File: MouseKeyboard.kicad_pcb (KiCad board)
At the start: 2 copper layers, 79.4 x 62.2 mm, 20 parts, among them IC1 ATMEGA328P-P, J1 USB, SW1 SW_PUSH, SW2 SW_PUSH, SW3 SW_PUSH, SW4 SW_PUSH, SW5 SW_PUSH, SW6 SW_PUSH, SW7 SW_PUSH, SW8 SPST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

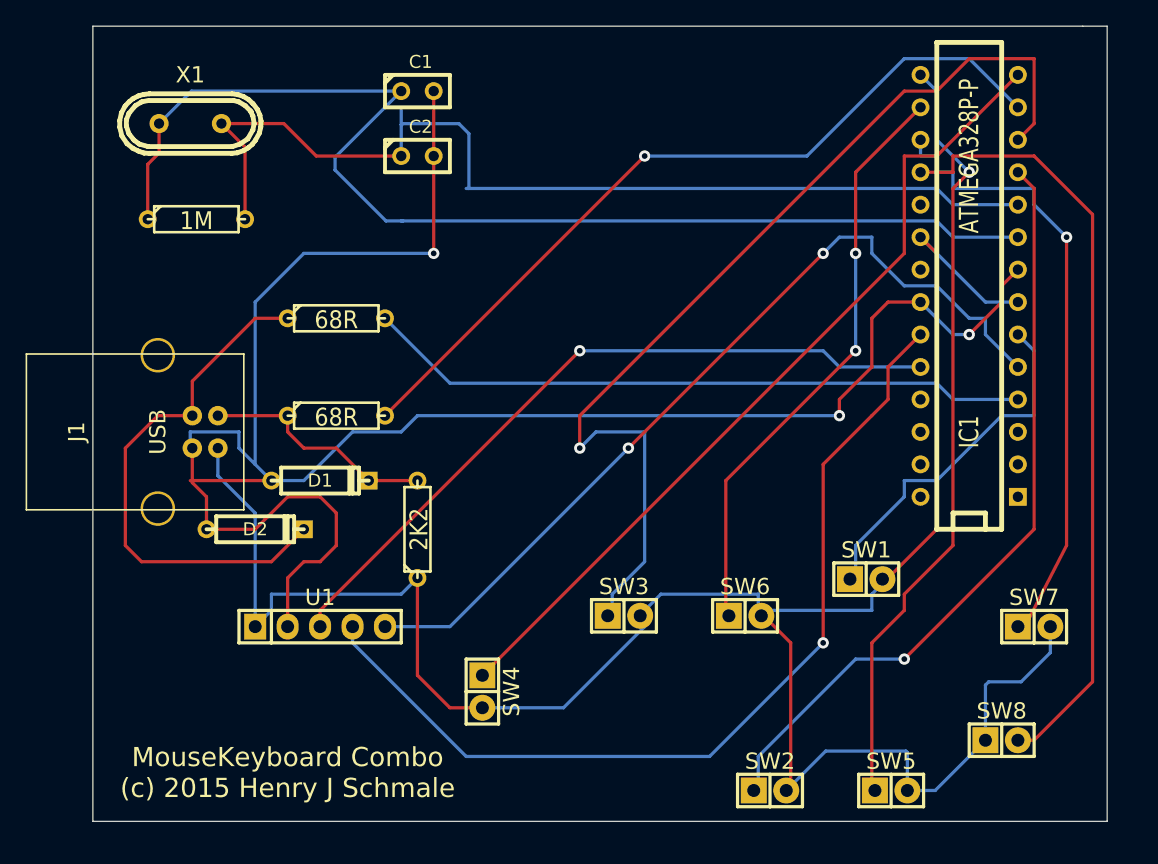
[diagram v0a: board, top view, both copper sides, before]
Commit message: Improved PCB Design
* Reduced Size of board by ~20%
* Rerouted, and it passes the design check
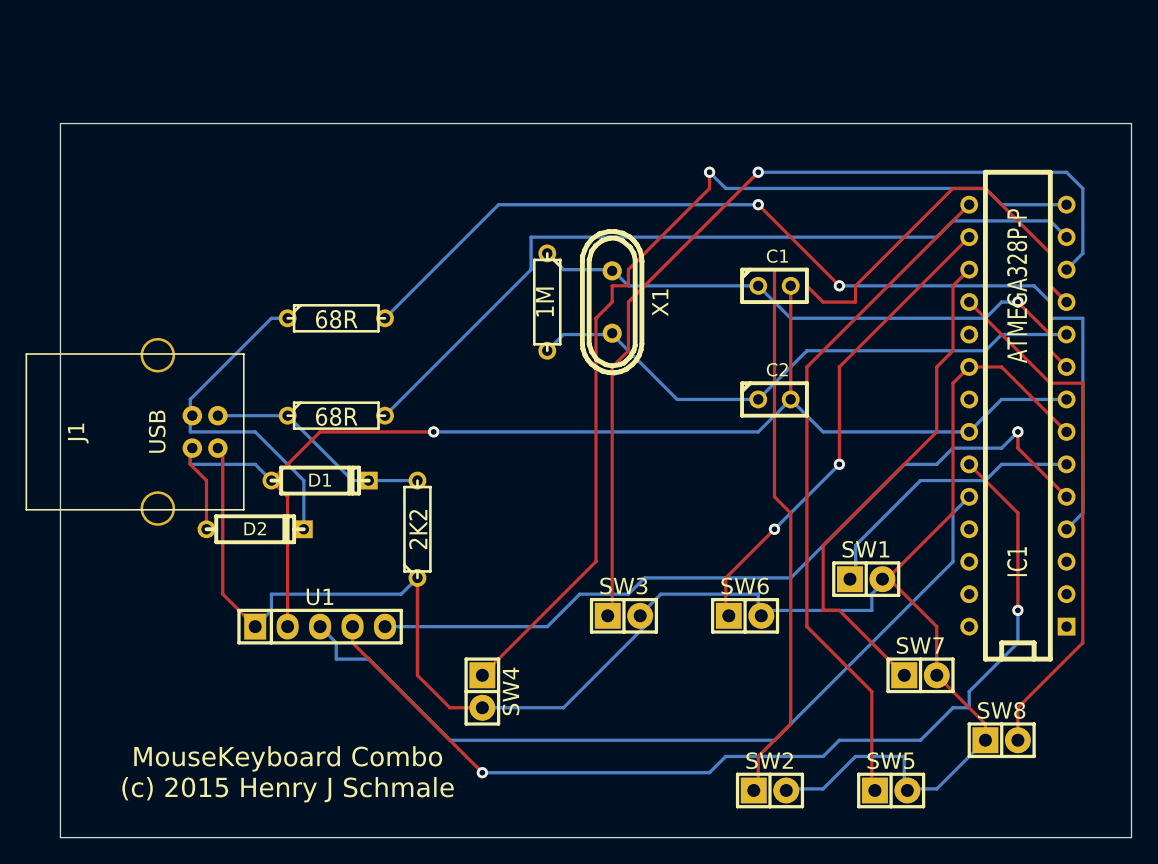
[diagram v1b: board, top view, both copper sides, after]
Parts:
- moved X1 35.9 mm to (142.2, 92.7), turned to 270 degrees
- moved C2 33.8 mm to (154.9, 100.3)
- moved C1 31.8 mm to (154.9, 91.4)
- moved R4 28.2 mm to (137.2, 92.7), turned to 270 degrees
- moved IC1 10.9 mm to (174.0, 101.6)
- moved SW7 9.67 mm to (166.4, 121.9)
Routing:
- net GND: track 158.2 -> 103.2 mm, vias 3 -> 1
- net XTAL1: track 92.1 -> 46.3 mm, vias 0 -> 1
- net XTAL2: track 81.0 -> 45.6 mm
- net Net-(IC1-Pad4): track 52.2 -> 79.8 mm, vias 0 -> 2
- net +5V: track 177.1 -> 152.9 mm
- net Net-(IC1-Pad18): track 61.4 -> 41.6 mm
- net Net-(IC1-Pad11): track 60.3 -> 76.8 mm, vias 1 -> 0
- net Net-(D2-Pad2): track 41.7 -> 27.4 mm
- net Net-(IC1-Pad14): track 65.8 -> 76.5 mm, vias 0 -> 1
- net Net-(IC1-Pad17): track 49.5 -> 39.9 mm, vias 1 -> 0
- net Net-(IC1-Pad16): track 46.2 -> 37.6 mm
- net Net-(IC1-Pad24): track 57.2 -> 65.3 mm, vias 1 -> 0
- net Net-(IC1-Pad15): track 60.9 -> 53.4 mm, vias 1 -> 0
- net Net-(IC1-Pad6): track 28.8 -> 22.1 mm
- net Net-(IC1-Pad5): track 67.9 -> 62.5 mm, vias 2 -> 1
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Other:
- board size 79.4 x 62.2 mm -> 83.8 x 55.9 mm

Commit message: Silkscreen More Stuff
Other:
- board text added: "+ G X Y S"
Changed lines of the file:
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@@
     (area 95.25 81.28 180.34 132.08)
     (thickness 1.6)
-    (drawings 7)
+    (drawings 8)
     (tracks 226)
     (zones 0)
@@
       (net 3 XTAL2))
   )
+  (gr_text "+ G X Y S\n" (at 113.03 120.65) (layer F.SilkS)
+    (effects (font (size 1.5 1.5) (thickness 0.3)) (justify left))
+  )
   (dimension 83.82 (width 0.3) (layer Dwgs.User)

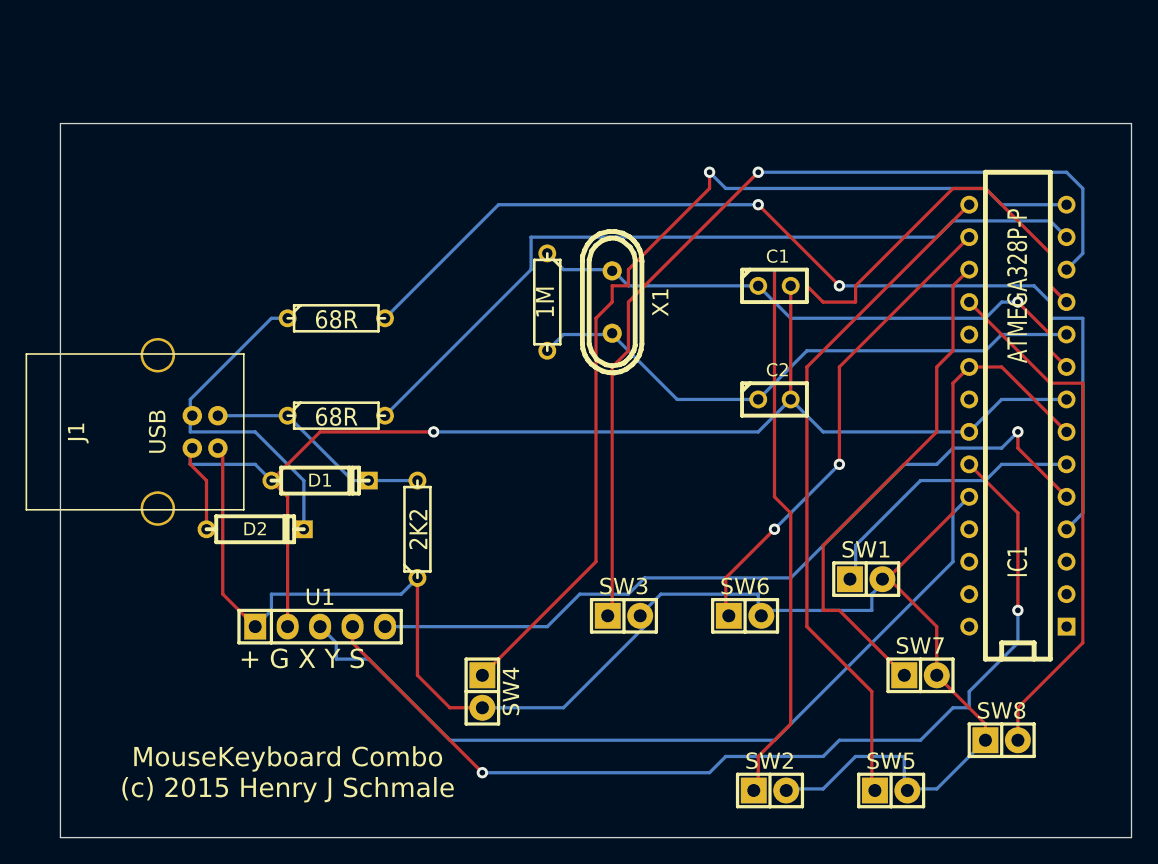
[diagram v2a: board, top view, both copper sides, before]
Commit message: Added Heat Conduction Plates all over the place
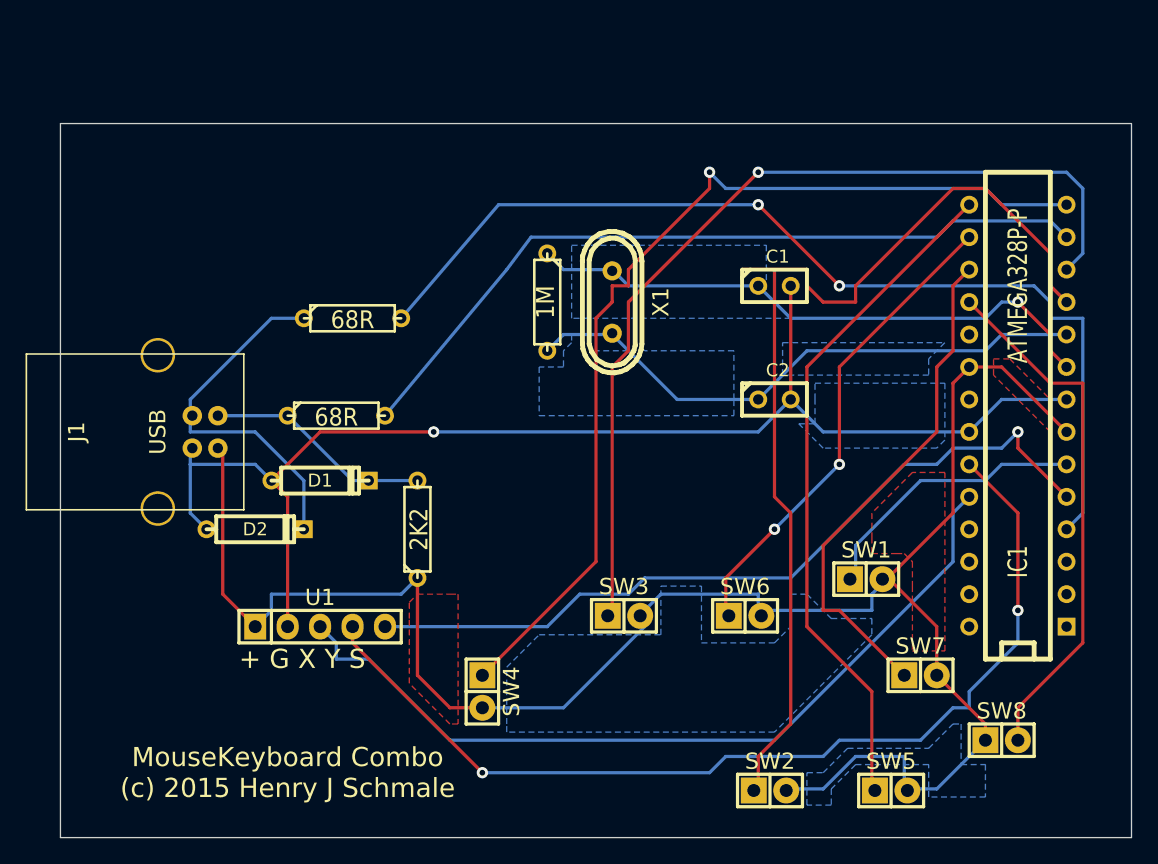
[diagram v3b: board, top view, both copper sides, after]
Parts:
- moved R2 1.27 mm to (121.9, 94.0)
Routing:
- net Net-(D2-Pad2): track 27.4 -> 28.7 mm
- net GND: track 103.2 -> 101.9 mm
- net Net-(IC1-Pad4): track 79.8 -> 78.9 mm
- net Net-(IC1-Pad13): track 61.7 -> 61.0 mm
- added copper zone on B.Cu, net +5V
- added copper zone on F.Cu, net +5V
- added copper zone on B.Cu, net GND
- added copper zone on B.Cu, net XTAL1
- added copper zone on B.Cu, net XTAL2
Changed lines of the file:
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@@
     (links 43)
     (no_connects 0)
-    (area 95.25 81.28 180.34 132.08)
+    (area 96.075499 78.689999 195.96 142.400001)
     (thickness 1.6)
     (drawings 8)
-    (tracks 226)
+    (tracks 225)
     (zones 0)
     (modules 20)
@@
     (trace_clearance 0.254)
     (zone_clearance 0.508)
-    (zone_45_only no)
+    (zone_45_only yes)
     (trace_min 0.254)
     (segment_width 0.2)
@@
   )
   (module Discret:R3 (layer F.Cu)
-    (at 120.65 93.98)
+    (at 121.92 93.98)
     (descr "Resitance 3 pas")
     (tags R)
@@
   (segment (start 138.43 90.17) (end 142.24 90.17) (width 0.254) (layer B.Cu) (net 1) (status 80000))
   (segment (start 142.24 90.17) (end 142.24 90.26906) (width 0.254) (layer B.Cu) (net 1) (status 80000))
+  (segment (start 109.22 105.41) (end 109.22 109.22) (width 0.254) (layer B.Cu) (net 2))
+  (segment (start 109.22 109.22) (end 110.49 110.49) (width 0.254) (layer B.Cu) (net 2))
   (segment (start 156.21 100.33) (end 153.67 102.87) (width 0.254) (layer B.Cu) (net 2) (status 80000))
   (segment (start 153.67 102.87) (end 128.27 102.87) (width 0.254) (layer B.Cu) (net 2) (status 80000))
@@
   (segment (start 116.84 107.95) (end 116.84 118.11) (width 0.254) (layer F.Cu) (net 2) (status 80000))
   (segment (start 109.38002 104.14) (end 109.22 104.14) (width 0.254) (layer F.Cu) (net 2) (status 80000))
-  (segment (start 109.22 104.14) (end 109.22 105.41) (width 0.254) (layer F.Cu) (net 2) (status 80000))
-  (segment (start 109.22 105.41) (end 110.49 106.68) (width 0.254) (layer F.Cu) (net 2) (status 80000))
-  (segment (start 110.49 106.68) (end 110.49 110.49) (width 0.254) (layer F.Cu) (net 2) (status 80000))
   (segment (start 156.21 91.44) (end 156.21 100.33) (width 0.254) (layer F.Cu) (net 2) (status 80000))
   (segment (start 153.67 100.33) (end 157.48 96.52) (width 0.254) (layer B.Cu) (net 3) (status 80000))
@@
   (segment (start 109.22 101.6) (end 109.22 100.33) (width 0.254) (layer B.Cu) (net 5) (status 80000))
   (segment (start 109.22 100.33) (end 115.57 93.98) (width 0.254) (layer B.Cu) (net 5) (status 80000))
-  (segment (start 115.57 93.98) (end 116.84 93.98) (width 0.254) (layer B.Cu) (net 5) (status 80000))
-  (segment (start 124.46 93.98) (end 133.35 85.09) (width 0.254) (layer B.Cu) (net 8) (status 80000))
+  (segment (start 115.57 93.98) (end 118.11 93.98) (width 0.254) (layer B.Cu) (net 5) (status 80020))
+  (segment (start 125.73 93.98) (end 133.35 85.09) (width 0.254) (layer B.Cu) (net 8) (status 80010))
   (segment (start 133.35 85.09) (end 153.67 85.09) (width 0.254) (layer B.Cu) (net 8) (status 80000))
   (via (at 153.67 85.09) (size 0.889) (layers F.Cu B.Cu) (net 8) (status 80000))
@@
   (segment (start 168.91 86.36) (end 167.64 87.63) (width 0.254) (layer B.Cu) (net 14) (status 80000))
   (segment (start 167.64 87.63) (end 135.89 87.63) (width 0.254) (layer B.Cu) (net 14) (status 80000))
-  (segment (start 135.89 87.63) (end 135.89 90.17) (width 0.254) (layer B.Cu) (net 14) (status 80000))
-  (segment (start 135.89 90.17) (end 124.46 101.6) (width 0.254) (layer B.Cu) (net 14) (status 80000))
+  (segment (start 135.89 87.63) (end 133.985 90.17) (width 0.254) (layer B.Cu) (net 14) (status 80000))
+  (segment (start 133.985 90.17) (end 124.46 101.6) (width 0.254) (layer B.Cu) (net 14) (status 80000))
   (segment (start 132.08 121.92) (end 140.97 113.03) (width 0.254) (layer F.Cu) (net 15) (status 80000))
   (segment (start 140.97 113.03) (end 140.97 93.98) (width 0.254) (layer F.Cu) (net 15) (status 80000))
@@
   (segment (start 120.65 120.65) (end 120.65 119.38) (width 0.254) (layer B.Cu) (net 24) (status 80000))
   (segment (start 120.65 119.38) (end 119.38 118.11) (width 0.254) (layer B.Cu) (net 24) (status 80000))
+  (zone (net 3) (net_name XTAL2) (layer B.Cu) (hatch edge 0.508)
+    (connect_pads (clearance 0.508))
+    (min_thickness 0.254)
+    (fill (arc_segments 16) (thermal_gap 0.508) (thermal_bridge_width 0.508))
+    (polygon
+      (pts
+        (xy 139.065 95.885) (xy 138.43 96.52) (xy 138.43 97.79) (xy 136.525 97.79) (xy 136.525 101.6)
+        (xy 151.765 101.6) (xy 151.765 100.33) (xy 151.765 96.52) (xy 144.78 96.52) (xy 144.145 95.885)
+        (xy 143.51 96.52) (xy 140.97 96.52) (xy 140.97 95.25) (xy 139.065 95.25)
+      )
+    )
+  )
+  (zone (net 1) (net_name XTAL1) (layer B.Cu) (hatch edge 0.508)
+    (connect_pads (clearance 0.508))
+    (min_thickness 0.254)
+    (fill (arc_segments 16) (thermal_gap 0.508) (thermal_bridge_width 0.508))
+    (polygon
+      (pts
+        (xy 139.065 90.17) (xy 139.065 89.535) (xy 139.065 88.265) (xy 154.305 88.265) (xy 154.305 92.075)
+        (xy 156.21 93.98) (xy 139.065 93.98) (xy 139.065 90.17)
+      )
+    )
+  )
+  (zone (net 3) (net_name XTAL2) (layer B.Cu) (hatch edge 0.508)
+    (connect_pads (clearance 0.508))
+    (min_thickness 0.254)
+    (fill (arc_segments 16) (thermal_gap 0.508) (thermal_bridge_width 0.508))
+    (polygon
+      (pts
+        (xy 168.275 95.885) (xy 167.005 97.155) (xy 167.005 98.425) (xy 155.575 98.425) (xy 155.575 95.885)
+      )
+    )
+  )
+  (zone (net 2) (net_name GND) (layer B.Cu) (hatch edge 0.508)
+    (connect_pads (clearance 0.508))
+    (min_thickness 0.254)
+    (fill (arc_segments 16) (thermal_gap 0.508) (thermal_bridge_width 0.508))
+    (polygon
+      (pts
+        (xy 158.115 99.06) (xy 168.275 99.06) (xy 168.275 103.505) (xy 167.64 104.14) (xy 158.75 104.14)
+        (xy 156.845 102.235) (xy 158.115 102.235) (xy 158.115 100.33)
+      )
+    )
+  )
+  (zone (net 11) (net_name +5V) (layer F.Cu) (hatch edge 0.508)
+    (connect_pads (clearance 0.508))
+    (min_thickness 0.254)
+    (fill (arc_segments 16) (thermal_gap 0.508) (thermal_bridge_width 0.508))
+    (polygon
+      (pts
+        (xy 162.56 112.395) (xy 164.465 112.395) (xy 165.1 112.395) (xy 165.735 113.03) (xy 165.735 114.935)
+        (xy 165.735 120.015) (xy 168.275 120.015) (xy 168.275 106.045) (xy 165.735 106.045) (xy 162.56 109.22)
+        (xy 162.56 111.125)
+      )
+    )
+  )
+  (zone (net 11) (net_name +5V) (layer F.Cu) (hatch edge 0.508)
+    (connect_pads (clearance 0.508))
+    (min_thickness 0.254)
+    (fill (arc_segments 16) (thermal_gap 0.508) (thermal_bridge_width 0.508))
+    (polygon
+      (pts
+        (xy 126.365 116.205) (xy 127 115.57) (xy 129.54 115.57) (xy 130.175 115.57) (xy 130.175 125.73)
+        (xy 129.54 125.73) (xy 126.365 122.555) (xy 126.365 117.475)
+      )
+    )
+  )
+  (zone (net 11) (net_name +5V) (layer B.Cu) (hatch edge 0.508)
+    (connect_pads (clearance 0.508))
+    (min_thickness 0.254)
+    (fill (arc_segments 16) (thermal_gap 0.508) (thermal_bridge_width 0.508))
+    (polygon
+      (pts
+        (xy 133.985 125.73) (xy 133.985 121.285) (xy 136.525 118.745) (xy 146.05 118.745) (xy 146.05 114.935)
+        (xy 149.225 114.935) (xy 149.225 119.38) (xy 154.94 119.38) (xy 156.21 118.11) (xy 156.21 115.57)
+        (xy 157.48 115.57) (xy 159.385 117.475) (xy 162.56 117.475) (xy 162.56 118.745) (xy 154.94 126.365)
+        (xy 133.985 126.365)
+      )
+    )
+  )
+  (zone (net 11) (net_name +5V) (layer F.Cu) (hatch edge 0.508)
+    (connect_pads (clearance 0.508))
+    (min_thickness 0.254)
+    (fill (arc_segments 16) (thermal_gap 0.508) (thermal_bridge_width 0.508))
+    (polygon
+      (pts
+        (xy 172.085 97.155) (xy 173.355 97.155) (xy 176.53 100.33) (xy 176.53 102.87) (xy 172.085 98.425)
+      )
+    )
+  )
+  (zone (net 11) (net_name +5V) (layer B.Cu) (hatch edge 0.508)
+    (connect_pads (clearance 0.508))
+    (min_thickness 0.254)
+    (fill (arc_segments 16) (thermal_gap 0.508) (thermal_bridge_width 0.508))
+    (polygon
+      (pts
+        (xy 171.45 131.445) (xy 167.005 131.445) (xy 167.005 128.905) (xy 161.29 128.905) (xy 159.385 130.81)
+        (xy 159.385 132.08) (xy 157.48 132.08) (xy 157.48 129.54) (xy 158.75 129.54) (xy 160.655 127.635)
+        (xy 167.005 127.635) (xy 168.91 125.73) (xy 169.545 125.73) (xy 169.545 128.905) (xy 171.45 128.905)
+      )
+    )
+  )
 )
